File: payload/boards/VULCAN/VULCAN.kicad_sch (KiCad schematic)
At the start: 70 parts, among them IC1 LT1001CS8#PBF, J1 XT60PW-M, J2 POWER, J3 I2C, J4 Serial, J5 SPI, J6 GPIO, J7 Screw_Terminal_01x06, J8 Screw_Terminal_01x06, U1 DS18B20, U2 AZ1117IH-5.0TRG1, U3 MPXV7002DP, U4 AP63357, U5 DEV-16771, U6 MAX31850KATB+T, U7 MAX31850KATB+T, U8 MAX31850KATB+T

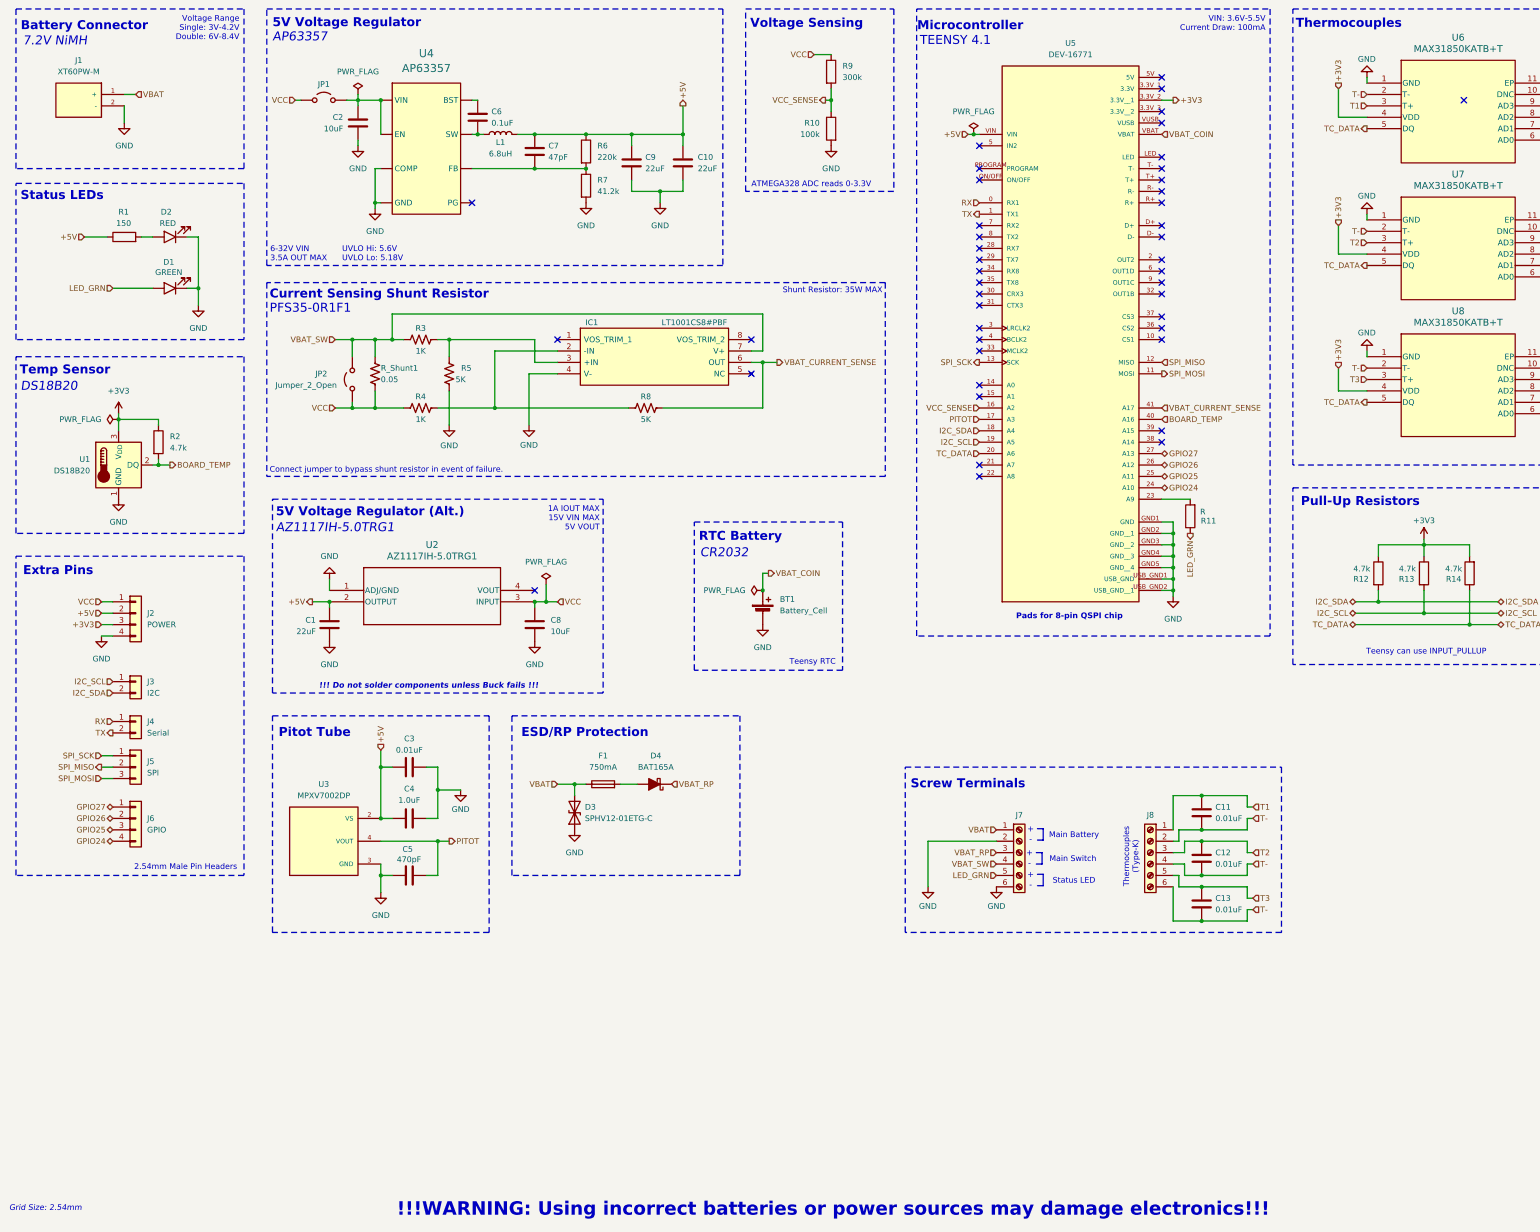
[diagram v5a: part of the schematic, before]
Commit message: updated BOM
distributor and manufacturer part number
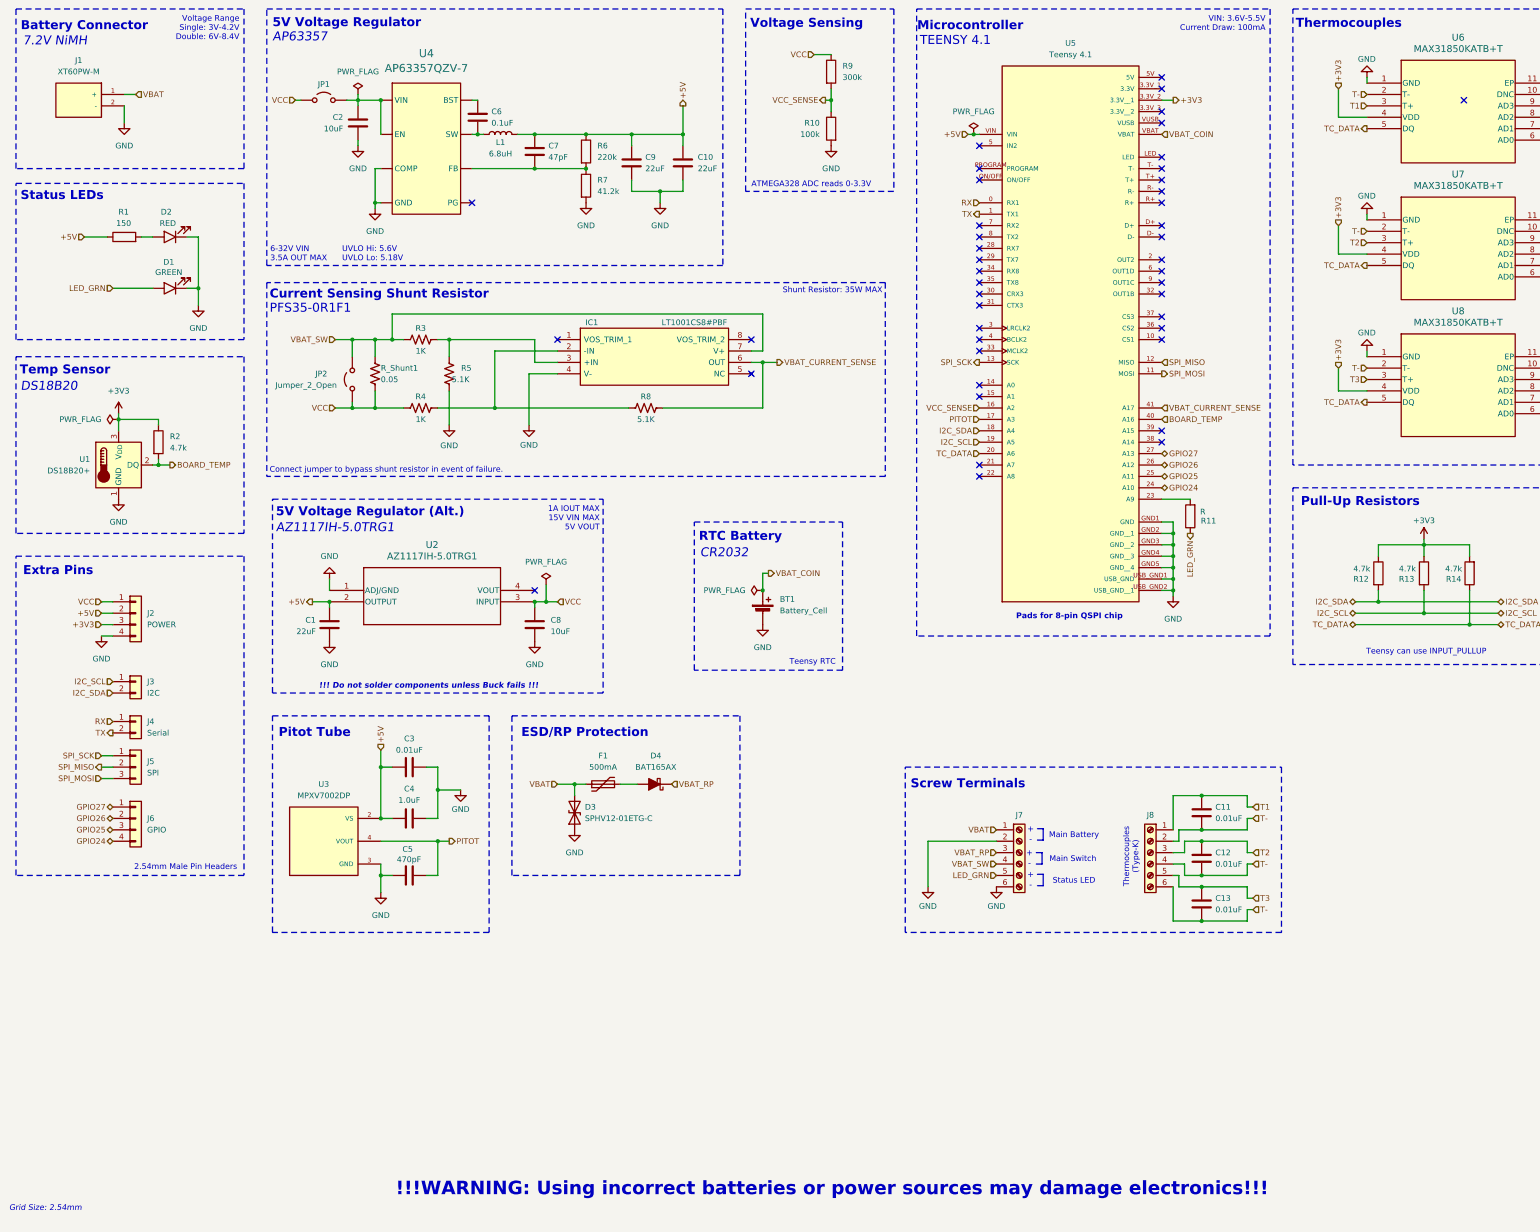
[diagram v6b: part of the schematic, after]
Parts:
- removed F1: 750mA, Fuse:Fuse_0805_2012Metric_Pad1.15x1.40mm_HandSolder, symbol Device:Fuse
- added F1: 500mA, Fuse:Fuse_1206_3216Metric_Pad1.42x1.75mm_HandSolder, symbol Device:Polyfuse
- BT1: Distributor (none) -> DigiKey; MPN (none) -> 1060
- C7: Distributor (none) -> DigiKey; MPN (none) -> CC0805JRNPO9BN470
- D1: Distributor (none) -> DigiKey; MPN (none) -> CMD17-21VGD/TR8
- D2: Distributor (none) -> DigiKey; MPN (none) -> CMD17-21VRD/TR8
- D3: Distributor (none) -> DigiKey; MPN (none) -> SPHV12-01ETG-C
- D4: value BAT165A -> BAT165AX; Distributor (none) -> DigiKey; MPN (none) -> BAT165AX
- HS1: Distributor (none) -> Sparkfun; MPN (none) -> PRT-18704
- IC1: MPN (none) -> LT1001CS8#PBF
- J2, J6: MPN (none) -> 0901471104
- J3, J4: MPN (none) -> 0901471102
- J5: MPN (none) -> 0901471103
- J7, J8: Distributor (none) -> DigiKey; MPN (none) -> OSTTE060104
- JP1, JP2, JP3, JP4, JP5, JP6: now left out of the parts list
- L1: Distributor (none) -> DigiKey; MPN (none) -> SRN8040TA-6R8M
- R1: Distributor (none) -> DigiKey; MPN (none) -> RC0805FR-07150RL
- R10: Distributor (none) -> DigiKey; MPN (none) -> RC0805FR-07100KL
- R12, R13, R14, R2: Distributor (none) -> DigiKey; MPN (none) -> RC0805FR-074K7L
- R3, R4: Distributor (none) -> DigiKey; MPN (none) -> RC0805FR-071KL
- R5, R8: value 5K -> 5.1K; Distributor (none) -> DigiKey; MPN (none) -> RC0805FR-075K1L
- R6: Distributor (none) -> DigiKey; MPN (none) -> RC0805JR-07220KL
- R7: Distributor (none) -> DigiKey; MPN (none) -> RC0805FR-0741K2L
- R9: Distributor (none) -> DigiKey; MPN (none) -> RC0805JR-07300KL
- R_Shunt1: Distributor (none) -> DigiKey; MPN (none) -> WSHP2818R0500FEA
- U1: value DS18B20 -> DS18B20+; Distributor (none) -> DigiKey; MPN (none) -> DS18B20+
- U2: Distributor (none) -> DigiKey; MPN (none) -> AZ1117IH-5.0TRG1
- U3: Distributor (none) -> DigiKey; MPN (none) -> MPXV7002DP
- U4: value AP63357 -> AP63357QZV-7; Distributor (none) -> DigiKey; MPN (none) -> AP63357QZV-7
- U5: value DEV-16771 -> Teensy 4.1; Distributor (none) -> SparkFun; MPN (none) -> DEV-16996
- U6, U7, U8: Distributor (none) -> DigiKey; MPN (none) -> MAX31850KATB+T
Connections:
- net VBAT: now also F1.1
- net at D4.2 (A): now also F1.2

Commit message: updates
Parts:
- removed R11: R, Resistor_SMD:R_0805_2012Metric_Pad1.20x1.40mm_HandSolder, symbol Device:R
- added R12: R, Resistor_SMD:R_0805_2012Metric_Pad1.20x1.40mm_HandSolder, symbol Device:R_Small
- added R2: 62, Resistor_SMD:R_0805_2012Metric_Pad1.20x1.40mm_HandSolder, symbol Device:R
- C1, C10, C9: Distributor (none) -> DigiKey; MPN (none) -> CC0805MKX5R8BB226
- C11, C12, C13, C3: Distributor (none) -> DigiKey; MPN (none) -> CC0805JRX7R9BB103
- C14, C15, C16, C6: Distributor (none) -> DigiKey; MPN (none) -> CC0805JRX7R9BB104
- C2, C8: Distributor (none) -> DigiKey; MPN (none) -> CC0805KKX5R8BB106
- C4: Distributor (none) -> DigiKey; MPN (none) -> CC0805JKX7R9BB105
- C5: Distributor (none) -> DigiKey; MPN (none) -> CC0805JRNPO9BN471
- IC1, J2, J3, J4, J5, J6: Distributor (none) -> DigiKey
- J1: Distributor (none) -> TME; MPN (none) -> XT60PW-M
- renumbered D2 to D1, D1 to D2, R9 to R10, R10 to R11, R12 to R13, R13 to R14, R14 to R15, R2 to R3, R3 to R4, R4 to R5, R5 to R6, R6 to R7, R7 to R8, R8 to R9
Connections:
- net LED_GRN: now also U5.15 (A1), R2.2; no longer D2.A, J7.5 (Pin_5)
- net LED_EXT: now reaches U5.23 (A9)
- net LED_EXT: now also R12.1
- new net: J7.5 (Pin_5), R12.2
- new net: D2.A, R2.1
- no-connect marks 47 -> 44
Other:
- moved on the sheet: C2, R9

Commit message: updated BOM
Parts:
- BT1: DKPN (none) -> 36-1060-ND
- C1, C10, C9: DKPN (none) -> 311-1903-1-ND
- C11, C12, C13, C3: DKPN (none) -> 311-1857-1-ND
- C14, C15, C16, C6: DKPN (none) -> 311-1858-1-ND
- C2, C8: DKPN (none) -> 311-1869-1-ND
- C4: DKPN (none) -> 311-3498-1-ND
- C5: DKPN (none) -> 311-1119-1-ND
- C7: DKPN (none) -> 311-1107-1-ND
- D1: DKPN 475-1278-1-ND -> L62501CT-ND
- D2: DKPN 475-1278-1-ND -> L62505CT-ND
- D3: DKPN (none) -> F6505CT-ND
- D4: DKPN (none) -> 1727-2752-1-ND
- F1: DKPN (none) -> F3733CT-ND
- IC1: DKPN (none) -> 505-LT1001CS8#PBF-ND
- J2, J6: DKPN (none) -> WM14831-ND
- J3, J4: DKPN (none) -> WM23663-ND
- J5: DKPN (none) -> WM14830-ND
- J7, J8: DKPN (none) -> ED2744-ND
- L1: DKPN (none) -> SRN8040TA-6R8MCT-ND
- R1: DKPN (none) -> 311-150CRCT-ND
- R10: DKPN (none) -> 311-300KARCT-ND
- R11: DKPN (none) -> 311-100KCRCT-ND
- R13, R14, R15, R3: DKPN (none) -> 311-4.70KCRCT-ND
- R2: DKPN (none) -> 311-62.0CRCT-ND
- R4, R5: DKPN (none) -> 311-1.00KCRCT-ND
- R6, R9: DKPN (none) -> 311-5.10KCRCT-ND
- R7: DKPN (none) -> 311-220KARCT-ND
- R8: DKPN (none) -> 311-41.2KCRCT-ND
- R_Shunt1: DKPN (none) -> 541-3281-1-ND
- U1: DKPN (none) -> DS18B20+-ND
- U2: DKPN (none) -> AZ1117IH-5.0TRG1DICT-ND
- U3: DKPN (none) -> MPXV7002DP-ND
- U4: DKPN (none) -> 31-AP63357QZV-7CT-ND
- U6, U7, U8: DKPN (none) -> MAX31850KATB+TCT-ND
